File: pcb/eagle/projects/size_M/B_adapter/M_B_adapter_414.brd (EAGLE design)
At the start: 8 parts

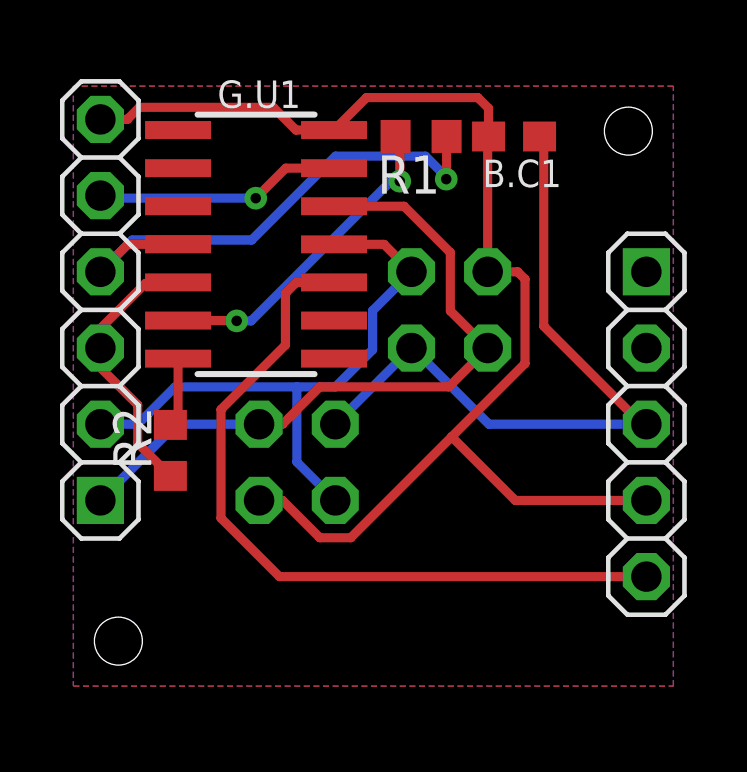
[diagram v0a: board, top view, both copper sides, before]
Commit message: updated for PCB version 4
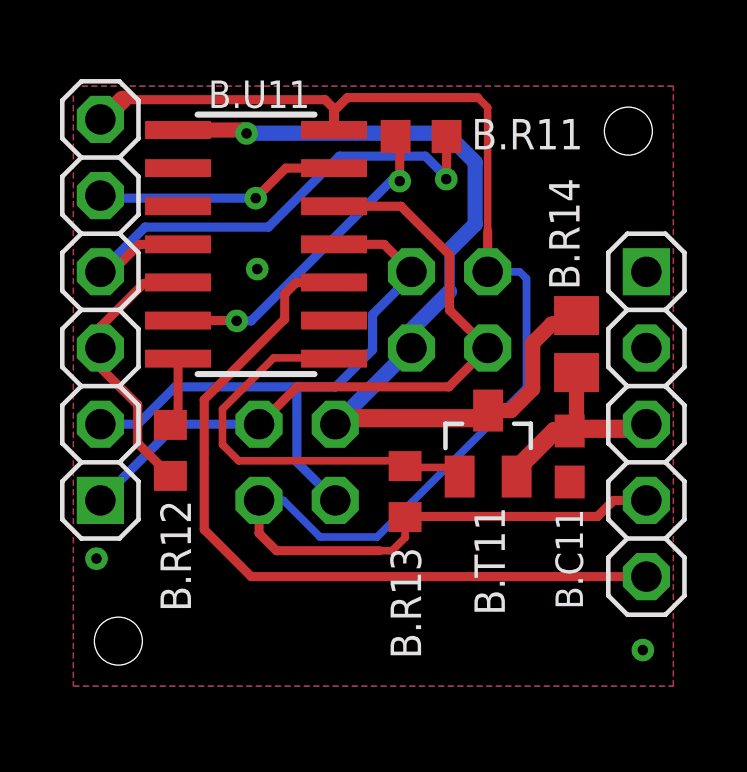
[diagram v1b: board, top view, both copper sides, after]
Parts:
- removed B.C1: 100n, rcl:C0603
- added B.C11: 100n, rcl:C0603
- added B.R13: 100k, rcl:R0603
- added B.R14: alternativ fuse or 0R, hugo:FUSE
- added B.T11: NX3008, hugo:SO23
- B.R11: value (none) -> alternative RX 0R
- B.R12: value (none) -> alternative TX 0R
- renumbered B.J2 to B.J12, B.J4 to B.J14, B.J5 to B.J11, G.U1 to B.U11, JB3 to B.J13, R1 to B.R11, R2 to B.R12
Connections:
- removed net 3V3: B.C1.1, B.J11.3, B.J13.1, B.J14.4
- new net N$3: B.R13.1, B.T11.G, B.U11.8
- new net N$4: B.C11.1, B.J11.3, B.R14.1, B.T11.S
- net GND: now also B.C11.2, B.R13.2; no longer B.C1.2
- net VCC: now also B.J13.1, B.J14.4, B.R14.2, B.T11.D
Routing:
- net VCC: track 0.00 -> 31.5 mm, vias 0 -> 1
- net 3V3: track 23.6 -> 0.00 mm
- net N$3: track 0.00 -> 14.1 mm
- net GND: track 42.8 -> 52.3 mm, vias 0 -> 3
- net N$4: track 0.00 -> 7.24 mm
- net UPDI: track 25.1 -> 26.2 mm
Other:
- board text added: "adapter 414 M.4"
- board text removed: "adapter414 M.3"

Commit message: collection of PCBs for v4 started
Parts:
- B.R11: value alternative RX 0R -> alt RX 0R
- B.R12: value alternative TX 0R -> alt TX 0R
- B.R14: value alternativ fuse or 0R -> alt fuse or 0R
- moved B.R12 0.55 mm to (3.86, 8.89)
- moved B.U11 0.23 mm to (6.59, 15.5)
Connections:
- new net VBAT: B.J11.2
- new net VUSB: B.J11.1
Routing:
- net GND: track 52.3 -> 51.8 mm, vias 3 -> 4

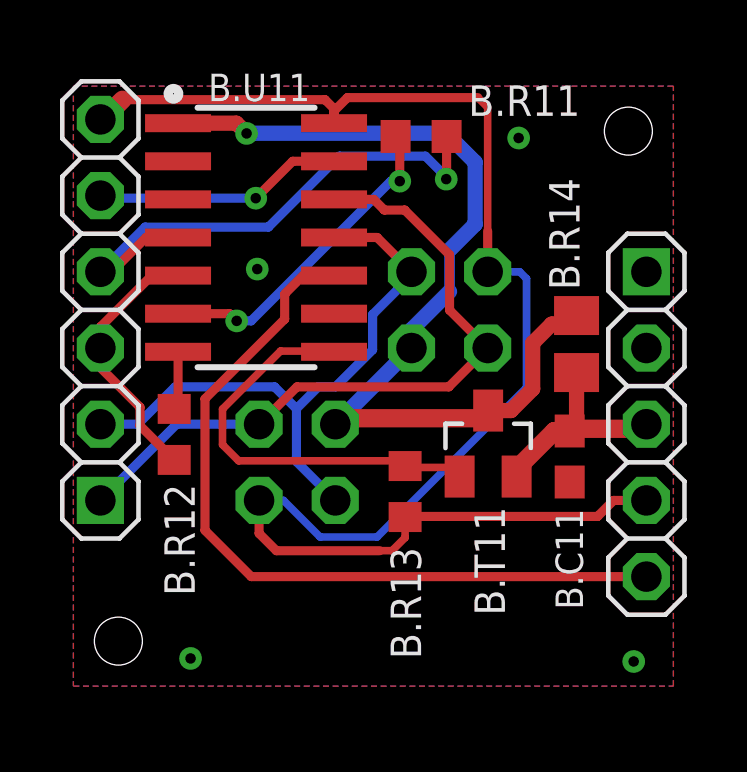
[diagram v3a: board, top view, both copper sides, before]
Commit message: bugfix: switched serial TX-RX
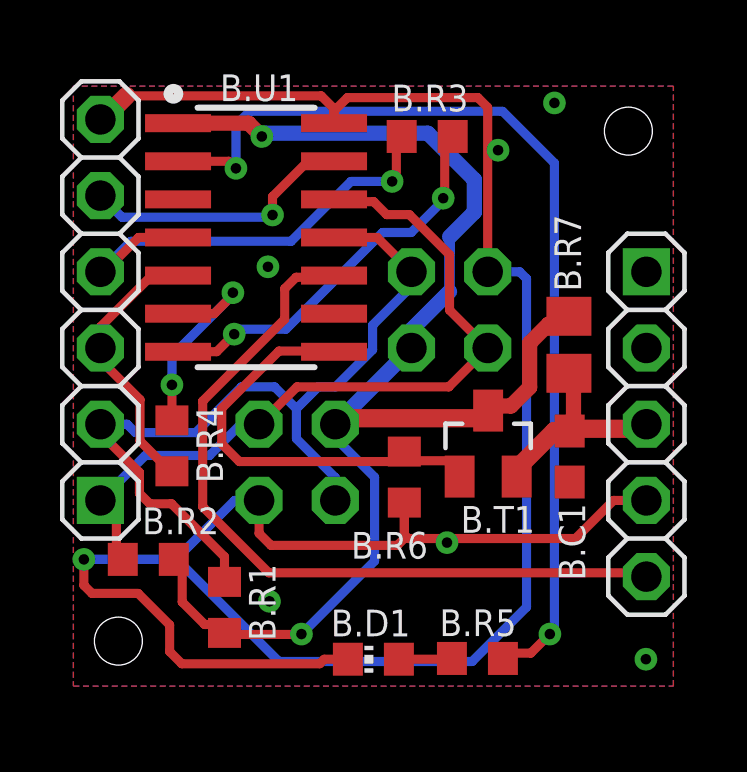
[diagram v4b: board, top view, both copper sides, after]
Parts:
- removed B.R11: alt RX 0R, rcl:R0603
- removed B.R12: alt TX 0R, rcl:R0603
- removed B.R13: 100k, rcl:R0603
- removed B.R14: alt fuse or 0R, hugo:FUSE
- added B.D1: (no value), led:CHIP-LED0603
- added B.R1, B.R2: 2k2, rcl:R0603
- added B.R3: alt RX 0R, rcl:R0603
- added B.R4: alt TX 0R, rcl:R0603
- added B.R5: 1k, rcl:R0603
- added B.R6: 100k, rcl:R0603
- added B.R7: alt fuse or 0R, hugo:FUSE
- renumbered B.C11 to B.C1, B.J11 to B.J1, B.J12 to B.J2, B.J13 to B.J3, B.J14 to B.J4, B.T11 to B.T1, B.U11 to B.U1
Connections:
- new net N$5: B.R5.2, B.U1.2
- new net PA1: B.D1.A1, B.R5.1
- net GND: now also B.D1.C1, B.R6.2; no longer B.R13.2
- net N$1: now also B.R4.2, B.U1.6; no longer B.R12.2, B.U1.7
- net N$2: now also B.R3.2, B.U1.7; no longer B.R11.2, B.U1.6
- net N$3: now also B.R6.1; no longer B.R13.1
- net N$4: now also B.R7.1; no longer B.R14.1
- net PA6: now also B.R3.1; no longer B.R11.1
- net PA7: now also B.R4.1; no longer B.R12.1
- net SCL: now also B.R2.1
- net SDA: now also B.R1.1
- net VCC: now also B.R1.2, B.R2.2, B.R7.2; no longer B.R14.2
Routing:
- net N$5: track 0.00 -> 32.7 mm, vias 0 -> 2
- net GND: track 51.8 -> 84.5 mm, vias 4 -> 7
- net VCC: track 31.5 -> 46.0 mm, vias 1 -> 2
- net SDA: track 20.5 -> 28.1 mm
- net N$1: track 1.96 -> 7.26 mm, vias 0 -> 2
- net PA6: track 18.0 -> 15.7 mm
- net N$2: track 11.0 -> 13.3 mm
- net SCL: track 23.3 -> 25.5 mm
- net PA1: track 0.00 -> 1.78 mm
- net PA3: track 8.33 -> 9.22 mm
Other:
- board text added: "adapter 414 M.6"
- board text removed: "adapter 414 M.4"

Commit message: minor changes for PCB v6.
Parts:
- removed B.C1: 100n, rcl:C0603
- removed B.D1: (no value), led:CHIP-LED0603
- removed B.R2: 2k2, rcl:R0603
- removed B.R3: alt RX 0R, rcl:R0603
- removed B.R4: alt TX 0R, rcl:R0603
- removed B.R5: 1k, rcl:R0603
- removed B.R7: alt fuse or 0R, hugo:FUSE
- added B.C11, B.C12: 100n, rcl:C0603
- added B.D11: (no value), led:CHIP-LED0603
- added B.R12: 2k2, rcl:R0603
- added B.R13: alt RX 0R, rcl:R0603
- added B.R14: alt TX 0R, rcl:R0603
- added B.R15: 1k, rcl:R0603
- added B.R17: alt fuse or 0R, hugo:FUSE
- renumbered B.R1 to B.R11, B.R6 to B.R16, B.T1 to B.T11, B.U1 to B.U11
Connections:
- net GND: now also B.C11.2, B.C12.2, B.D11.C1; no longer B.C1.2, B.D1.C1
- net N$1: now also B.R14.2; no longer B.R4.2
- net N$2: now also B.R13.2; no longer B.R3.2
- net N$4: now also B.C11.1, B.R17.1; no longer B.C1.1, B.R7.1
- net N$5: now also B.R15.2; no longer B.R5.2
- net PA1: now also B.D11.A1, B.R15.1; no longer B.D1.A1, B.R5.1
- net PA6: now also B.R13.1; no longer B.R3.1
- net PA7: now also B.R14.1; no longer B.R4.1
- net SCL: now also B.R12.1; no longer B.R2.1
- net VCC: now also B.C12.1, B.R12.2, B.R17.2; no longer B.R2.2, B.R7.2
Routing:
- net VCC: track 46.0 -> 81.2 mm, vias 2 -> 4
- net SCL: track 25.5 -> 46.1 mm
- net SDA: track 28.1 -> 43.7 mm
- net PA6: track 15.7 -> 17.6 mm
- net N$5: track 32.7 -> 31.1 mm
- net N$4: track 7.24 -> 7.96 mm
- net GND: track 84.5 -> 83.8 mm
- net N$1: track 7.26 -> 7.79 mm
